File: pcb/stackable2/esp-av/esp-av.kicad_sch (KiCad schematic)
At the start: 44 parts, among them J0 DC-005, J1 USB_C_Receptacle_USB2.0_16P, J10 JST SH, J11 STEMMA-Signal, Q1 PDNM6ET20V05, SW1 Reset, SW2 Boot, U1 USBLC6-2P6, U11 SN74LVC1T45Z6, U2 ME6211C33M5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

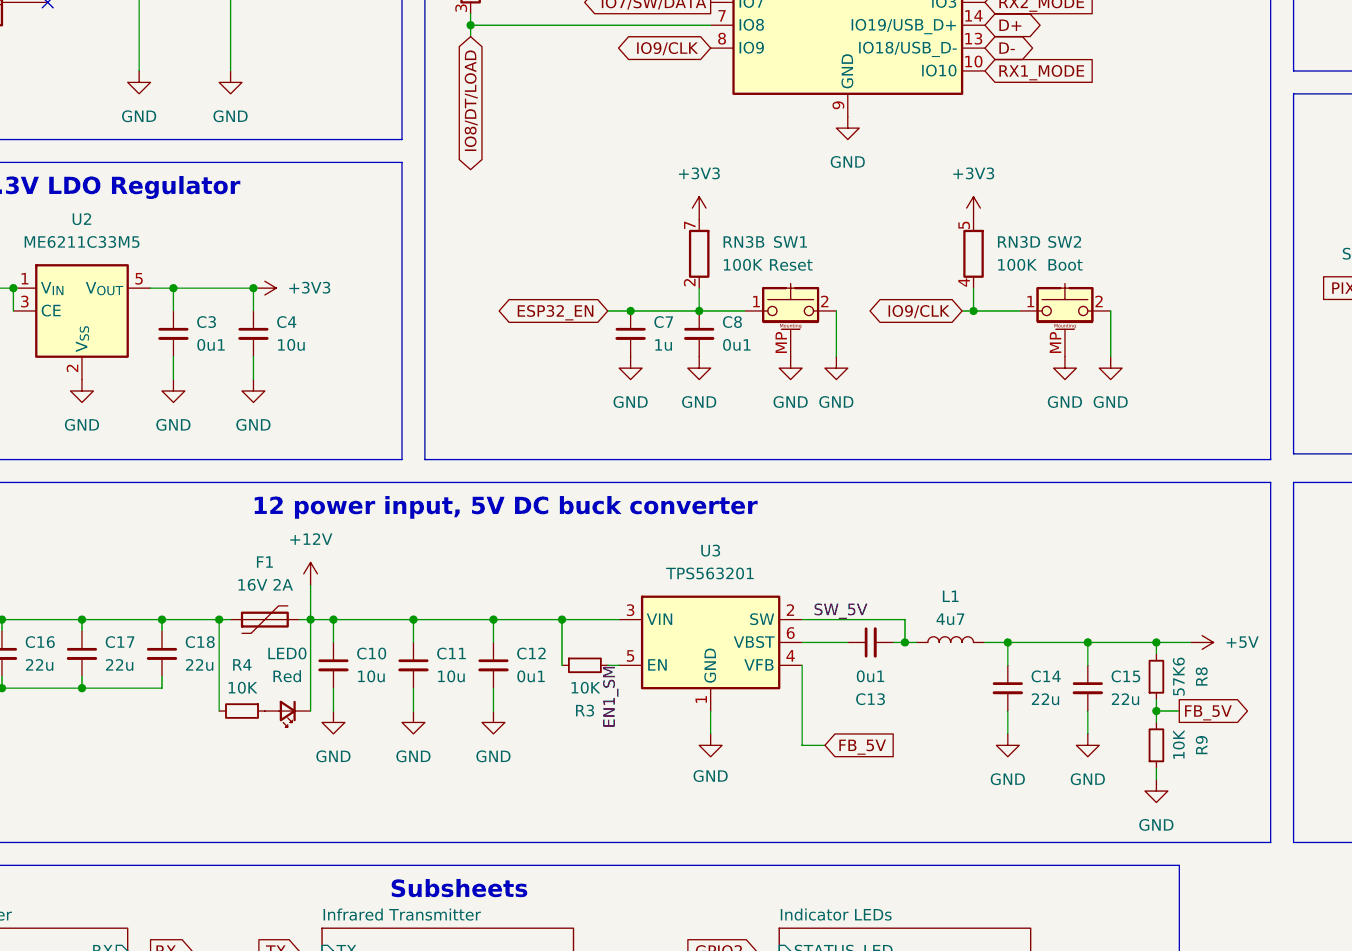
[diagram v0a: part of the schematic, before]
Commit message: Reroute buck IC enable trace, tweak schematic placements for readability
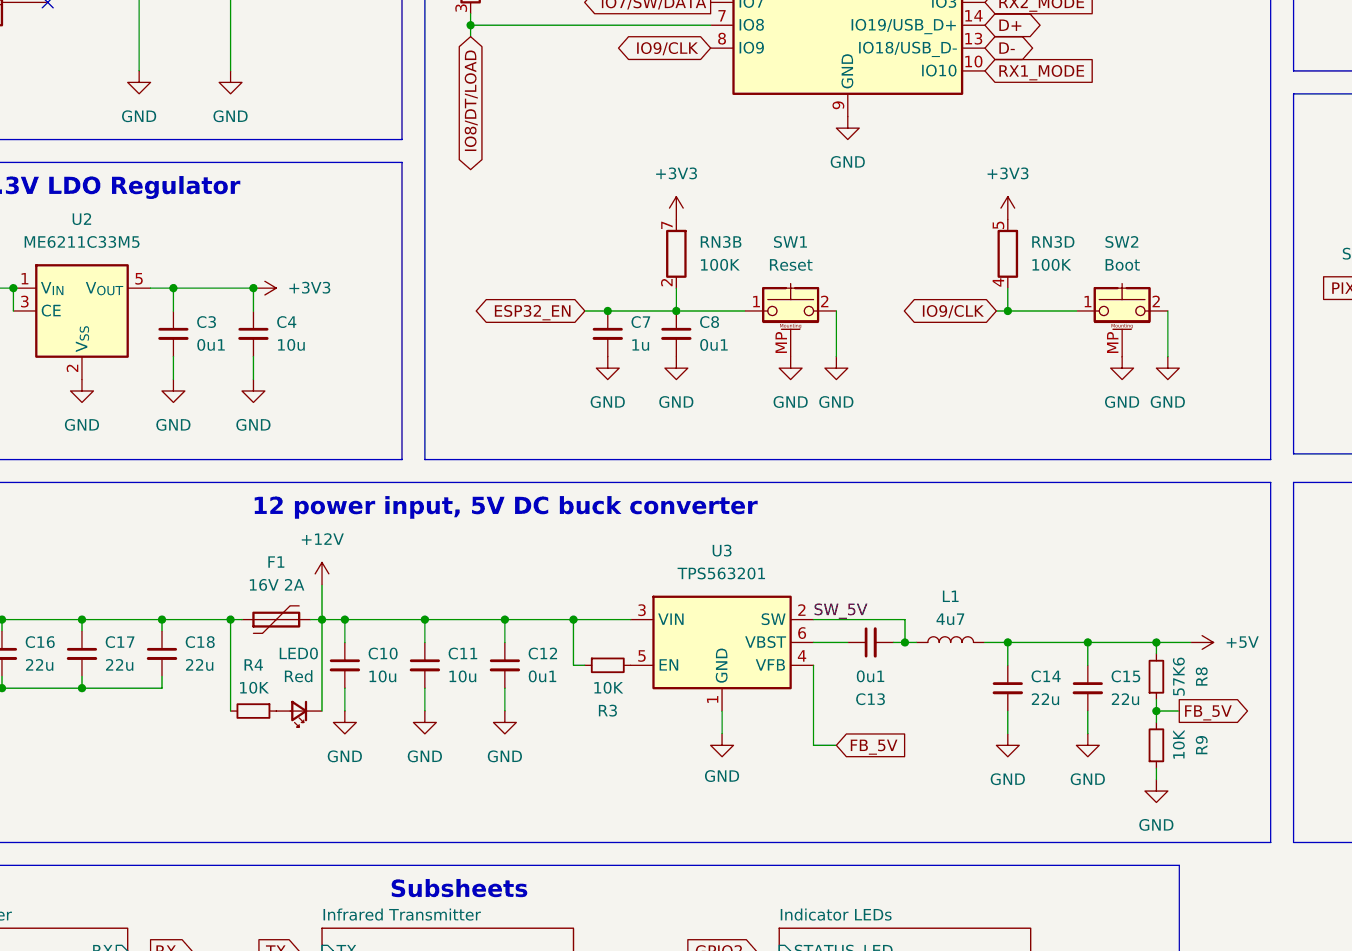
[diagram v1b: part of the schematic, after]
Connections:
- net EN1_SM: no longer names the net of R3.2, U3.5 (EN)
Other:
- moved on the sheet: C10, C11, C12, C7, C8, F1, LED0, R3, R4, RN3B, RN3D, SW2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

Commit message: Change esp-av boot tactile button type
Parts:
- removed SW2: Boot, electromechanical:SW_Push_1P1T_NO_3.3x3.3mm_MP, symbol electromechanical:SW_Push_MountingPin
- added SW2: Boot, Button_Switch_SMD:SW_SPST_TL3342, symbol Switch:SW_Push
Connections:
- net ESP32_EN: now also RN3.3 (R3.1); no longer RN3.2 (R2.1)
- net GND: now also SW2.2
- net IO8/DT/LOAD: now also RN3.2 (R2.1); no longer RN3.3 (R3.1)
- net IO9/CLK: now also SW2.1
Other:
- moved on the sheet: RN3B, RN3C
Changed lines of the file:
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@@
 	)
 	(symbol
+		(lib_id "Switch:SW_Push")
+		(at 168.91 95.25 0)
+		(unit 1)
+		(exclude_from_sim no)
+		(in_bom yes)
+		(on_board yes)
+		(dnp no)
+		(fields_autoplaced yes)
+		(property "Reference" "SW2"
+			(at 168.91 87.63 0)
+			(effects
+				(font
+					(size 1.27 1.27)
+				)
+			)
+		)
+		(property "Value" "Boot"
+			(at 168.91 90.17 0)
+			(effects
+				(font
+					(size 1.27 1.27)
+				)
+			)
+		)
+		(property "Footprint" "Button_Switch_SMD:SW_SPST_TL3342"
+			(at 168.91 90.17 0)
+			(effects
+				(font
+					(size 1.27 1.27)
+				)
+				(hide yes)
+			)
+		)
+		(property "Datasheet" "~"
+			(at 168.91 90.17 0)
+			(effects
+				(font
+					(size 1.27 1.27)
+				)
+				(hide yes)
+			)
+		)
+		(property "Description" "Push button switch, generic, two pins"
+			(at 168.91 95.25 0)
+			(effects
+				(font
+					(size 1.27 1.27)
+				)
+				(hide yes)
+			)
+		)
+		(pin "2"
+		)
+		(pin "1"
+		)
+		(instances
+			(project ""
+				(path "/76a56607-25e2-40a3-9282-ff279b153f75"
+					(reference "SW2")
+					(unit 1)
+				)
+			)
+		)
+	)
+	(symbol
 		(lib_id "Connector_Generic_MountingPin:Conn_01x05_MountingPin")
 		(at 223.52 132.08 0)
@@
 	(symbol
 		(lib_id "Device:R_Pack04_Split")
-		(at 96.52 58.42 0)
+		(at 119.38 88.9 0)
 		(unit 3)
 		(exclude_from_sim no)
@@
 		(fields_autoplaced yes)
 		(property "Reference" "RN3"
-			(at 99.06 57.1499 0)
+			(at 121.92 87.6299 0)
 			(effects
 				(font
@@
 		)
 		(property "Value" "100K"
-			(at 99.06 59.6899 0)
+			(at 121.92 90.1699 0)
 			(effects
 				(font
@@
 		)
 		(property "Footprint" "discrete:R_Array_Convex_4x0603_HandSolder"
-			(at 94.488 58.42 90)
+			(at 117.348 88.9 90)
 			(effects
 				(font
@@
 		)
 		(property "Datasheet" "~"
-			(at 96.52 58.42 0)
+			(at 119.38 88.9 0)
 			(effects
 				(font
@@
 		)
 		(property "Description" "4 resistor network, parallel topology, split"
-			(at 96.52 58.42 0)
+			(at 119.38 88.9 0)
 			(effects
 				(font
@@
 	)
 	(symbol
-		(lib_id "power:GND")
-		(at 168.91 100.33 0)
-		(unit 1)
-		(exclude_from_sim no)
-		(in_bom yes)
-		(on_board yes)
-		(dnp no)
-		(fields_autoplaced yes)
-		(property "Reference" "#PWR019"
-			(at 168.91 106.68 0)
-			(effects
-				(font
-					(size 1.27 1.27)
-				)
-				(hide yes)
-			)
-		)
-		(property "Value" "GND"
-			(at 168.91 105.41 0)
-			(effects
-				(font
-					(size 1.27 1.27)
-				)
-			)
-		)
-		(property "Footprint" ""
-			(at 168.91 100.33 0)
-			(effects
-				(font
-					(size 1.27 1.27)
-				)
-				(hide yes)
-			)
-		)
-		(property "Datasheet" ""
-			(at 168.91 100.33 0)
-			(effects
-				(font
-					(size 1.27 1.27)
-				)
-				(hide yes)
-			)
-		)
-		(property "Description" "Power symbol creates a global label with name \"GND\" , ground"
-			(at 168.91 100.33 0)
-			(effects
-				(font
-					(size 1.27 1.27)
-				)
-				(hide yes)
-			)
-		)
-		(pin "1"
-		)
-		(instances
-			(project "esp-av"
-				(path "/76a56607-25e2-40a3-9282-ff279b153f75"
-					(reference "#PWR019")
-					(unit 1)
-				)
-			)
-		)
-	)
-	(symbol
 		(lib_id "Jumper:SolderJumper_3_Bridged12")
 		(at 241.3 96.52 180)
@@
 	)
 	(symbol
-		(lib_id "electromechanical:SW_Push_MountingPin")
-		(at 168.91 95.25 0)
-		(unit 1)
-		(exclude_from_sim no)
-		(in_bom yes)
-		(on_board yes)
-		(dnp no)
-		(fields_autoplaced yes)
-		(property "Reference" "SW2"
-			(at 168.91 87.63 0)
-			(effects
-				(font
-					(size 1.27 1.27)
-				)
-			)
-		)
-		(property "Value" "Boot"
-			(at 168.91 90.17 0)
-			(effects
-				(font
-					(size 1.27 1.27)
-				)
-			)
-		)
-		(property "Footprint" "electromechanical:SW_Push_1P1T_NO_3.3x3.3mm_MP"
-			(at 168.91 90.17 0)
-			(effects
-				(font
-					(size 1.27 1.27)
-				)
-				(hide yes)
-			)
-		)
-		(property "Datasheet" "~"
-			(at 168.91 90.17 0)
-			(effects
-				(font
-					(size 1.27 1.27)
-				)
-				(hide yes)
-			)
-		)
-		(property "Description" "Generic push-button switch, two contact pins and mounting pin(s)"
-			(at 168.91 95.25 0)
-			(effects
-				(font
-					(size 1.27 1.27)
-				)
-				(hide yes)
-			)
-		)
-		(pin "MP"
-		)
-		(pin "1"
-		)
-		(pin "2"
-		)
-		(instances
-			(project "esp-av"
-				(path "/76a56607-25e2-40a3-9282-ff279b153f75"
-					(reference "SW2")
-					(unit 1)
-				)
-			)
-		)
-	)
-	(symbol
 		(lib_id "power:GND")
 		(at 38.1 102.87 0)
@@
 	(symbol
 		(lib_id "Device:R_Pack04_Split")
-		(at 119.38 88.9 0)
+		(at 96.52 58.42 0)
 		(unit 2)
 		(exclude_from_sim no)
@@
 		(fields_autoplaced yes)
 		(property "Reference" "RN3"
-			(at 121.92 87.6299 0)
+			(at 99.06 57.1499 0)
 			(effects
 				(font
@@
 		)
 		(property "Value" "100K"
-			(at 121.92 90.1699 0)
+			(at 99.06 59.6899 0)
 			(effects
 				(font
@@
 		)
 		(property "Footprint" "discrete:R_Array_Convex_4x0603_HandSolder"
-			(at 117.348 88.9 90)
+			(at 94.488 58.42 90)
 			(effects
 				(font
@@
 		)
 		(property "Datasheet" "~"
-			(at 119.38 88.9 0)
+			(at 96.52 58.42 0)
 			(effects
 				(font
@@
 		)
 		(property "Description" "4 resistor network, parallel topology, split"
-			(at 119.38 88.9 0)
+			(at 96.52 58.42 0)
 			(effects
 				(font
